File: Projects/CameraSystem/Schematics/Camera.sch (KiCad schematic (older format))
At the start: 10 parts, among them J10 Conn_02x02_Odd_Even, J9 Conn_02x02_Odd_Even, Q2 BC846B_215, U6 OV7670, U7 SIT2001BI-S2-33E-24.000000G

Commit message: feat: symbol assignment updated
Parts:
- C21, C22: footprint Capacitor_SMD:C_0603_1608Metric_Pad1.05x0.95mm_HandSolder -> digikey-footprints:0603
- R26, R27, R28: footprint Resistor_SMD:R_0603_1608Metric_Pad1.05x0.95mm_HandSolder -> digikey-footprints:0603
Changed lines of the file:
@@
 F 0 "C21" H 4825 2300 50  0000 L CNN
 F 1 "100n" H 4825 2100 50  0000 L CNN
-F 2 "Capacitor_SMD:C_0603_1608Metric_Pad1.05x0.95mm_HandSolder" H 4838 2050 50  0001 C CNN
+F 2 "digikey-footprints:0603" H 4838 2050 50  0001 C CNN
 F 3 "" H 4800 2200 50  0001 C CNN
 	1    4800 2200
@@
 F 0 "C22" H 6525 4450 50  0000 L CNN
 F 1 "100n" H 6525 4250 50  0000 L CNN
-F 2 "Capacitor_SMD:C_0603_1608Metric_Pad1.05x0.95mm_HandSolder" H 6538 4200 50  0001 C CNN
+F 2 "digikey-footprints:0603" H 6538 4200 50  0001 C CNN
 F 3 "" H 6500 4350 50  0001 C CNN
 	1    6500 4350
@@
 F 0 "R26" V 8330 4700 50  0000 C CNN
 F 1 "10k" V 8250 4700 50  0000 C CNN
-F 2 "Resistor_SMD:R_0603_1608Metric_Pad1.05x0.95mm_HandSolder" V 8180 4700 50  0001 C CNN
+F 2 "digikey-footprints:0603" V 8180 4700 50  0001 C CNN
 F 3 "" H 8250 4700 50  0001 C CNN
 	1    8250 4700
@@
 F 0 "R27" V 8830 5500 50  0000 C CNN
 F 1 "10k" V 8750 5500 50  0000 C CNN
-F 2 "Resistor_SMD:R_0603_1608Metric_Pad1.05x0.95mm_HandSolder" V 8680 5500 50  0001 C CNN
+F 2 "digikey-footprints:0603" V 8680 5500 50  0001 C CNN
 F 3 "" H 8750 5500 50  0001 C CNN
 	1    8750 5500
@@
 F 0 "R28" V 9130 5250 50  0000 C CNN
 F 1 "4k7" V 9050 5250 50  0000 C CNN
-F 2 "Resistor_SMD:R_0603_1608Metric_Pad1.05x0.95mm_HandSolder" V 8980 5250 50  0001 C CNN
+F 2 "digikey-footprints:0603" V 8980 5250 50  0001 C CNN
 F 3 "" H 9050 5250 50  0001 C CNN
 	1    9050 5250

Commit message: feat: assign footprints
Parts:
- J10, J9: footprint (none) -> Pin_Headers:Pin_Header_Straight_2x02_Pitch2.54mm_SMD
- U6: footprint (none) -> Pin_Headers:Pin_Header_Straight_2x16_Pitch2.54mm
- U7: footprint (none) -> custom-footprints:SiT2001B_SOT23
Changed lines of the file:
@@
 $Descr A4 11693 8268
 encoding utf-8
-Sheet 6 9
+Sheet 5 9
 Title ""
 Date ""
@@
 F 0 "U6" H 5350 2550 60  0000 C CNN
 F 1 "OV7670" H 5350 3550 60  0000 C CNN
-F 2 "" H 5350 3050 60  0001 C CNN
+F 2 "Pin_Headers:Pin_Header_Straight_2x16_Pitch2.54mm" H 5350 3050 60  0001 C CNN
 F 3 "" H 5350 3050 60  0001 C CNN
 	1    5350 3050
@@
 F 0 "U7" H 7700 3700 60  0000 C CNN
 F 1 "SIT2001BI-S2-33E-24.000000G" H 7700 4550 60  0000 C CNN
-F 2 "" H 7700 4050 60  0001 C CNN
+F 2 "custom-footprints:SiT2001B_SOT23" H 7700 4050 60  0001 C CNN
 F 3 "" H 7700 4050 60  0001 C CNN
 	1    7700 4050
@@
 F 0 "J9" H 2700 1717 50  0000 C CNN
 F 1 "Conn_02x02_Odd_Even" H 2700 1626 50  0000 C CNN
-F 2 "" H 2650 1500 50  0001 C CNN
+F 2 "Pin_Headers:Pin_Header_Straight_2x02_Pitch2.54mm_SMD" H 2650 1500 50  0001 C CNN
 F 3 "~" H 2650 1500 50  0001 C CNN
 	1    2650 1500
@@
 F 0 "J10" H 7750 3167 50  0000 C CNN
 F 1 "Conn_02x02_Odd_Even" H 7750 3076 50  0000 C CNN
-F 2 "" H 7700 2950 50  0001 C CNN
+F 2 "Pin_Headers:Pin_Header_Straight_2x02_Pitch2.54mm_SMD" H 7700 2950 50  0001 C CNN
 F 3 "~" H 7700 2950 50  0001 C CNN
 	1    7700 2950

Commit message: feat: start layout
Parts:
- U6: footprint Pin_Headers:Pin_Header_Straight_2x16_Pitch2.54mm -> Pin_Headers:Pin_Header_Straight_2x08_Pitch2.54mm
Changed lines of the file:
@@
 F 0 "U6" H 5350 2550 60  0000 C CNN
 F 1 "OV7670" H 5350 3550 60  0000 C CNN
-F 2 "Pin_Headers:Pin_Header_Straight_2x16_Pitch2.54mm" H 5350 3050 60  0001 C CNN
+F 2 "Pin_Headers:Pin_Header_Straight_2x08_Pitch2.54mm" H 5350 3050 60  0001 C CNN
 F 3 "" H 5350 3050 60  0001 C CNN
 	1    5350 3050

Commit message: linux adaptation
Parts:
- U6: symbol cl-integrated_circuits:OV7670 -> CameraSystem-rescue:OV7670-cl-integrated_circuits
- U7: symbol cl-integrated_circuits:SIT2001BI-S2-33E-24.000000G -> CameraSystem-rescue:SIT2001BI-S2-33E-24.000000G-cl-integrated_circuits
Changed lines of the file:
@@
 $EndDescr
 $Comp
-L cl-integrated_circuits:OV7670 U6
+L CameraSystem-rescue:OV7670-cl-integrated_circuits U6
 U 1 1 5BBB684E
 P 5350 3050
+AR Path="/5BBB684E" Ref="U6"  Part="1"
+AR Path="/5BB4DA63/5BBB684E" Ref="U6"  Part="1"
 F 0 "U6" H 5350 2550 60  0000 C CNN
 F 1 "OV7670" H 5350 3550 60  0000 C CNN
@@
 CAM_CLK
 $Comp
-L cl-integrated_circuits:SIT2001BI-S2-33E-24.000000G U7
+L CameraSystem-rescue:SIT2001BI-S2-33E-24.000000G-cl-integrated_circuits U7
 U 1 1 5BBBA2DE
 P 7700 4050
+AR Path="/5BBBA2DE" Ref="U7"  Part="1"
+AR Path="/5BB4DA63/5BBBA2DE" Ref="U7"  Part="1"
 F 0 "U7" H 7700 3700 60  0000 C CNN
 F 1 "SIT2001BI-S2-33E-24.000000G" H 7700 4550 60  0000 C CNN

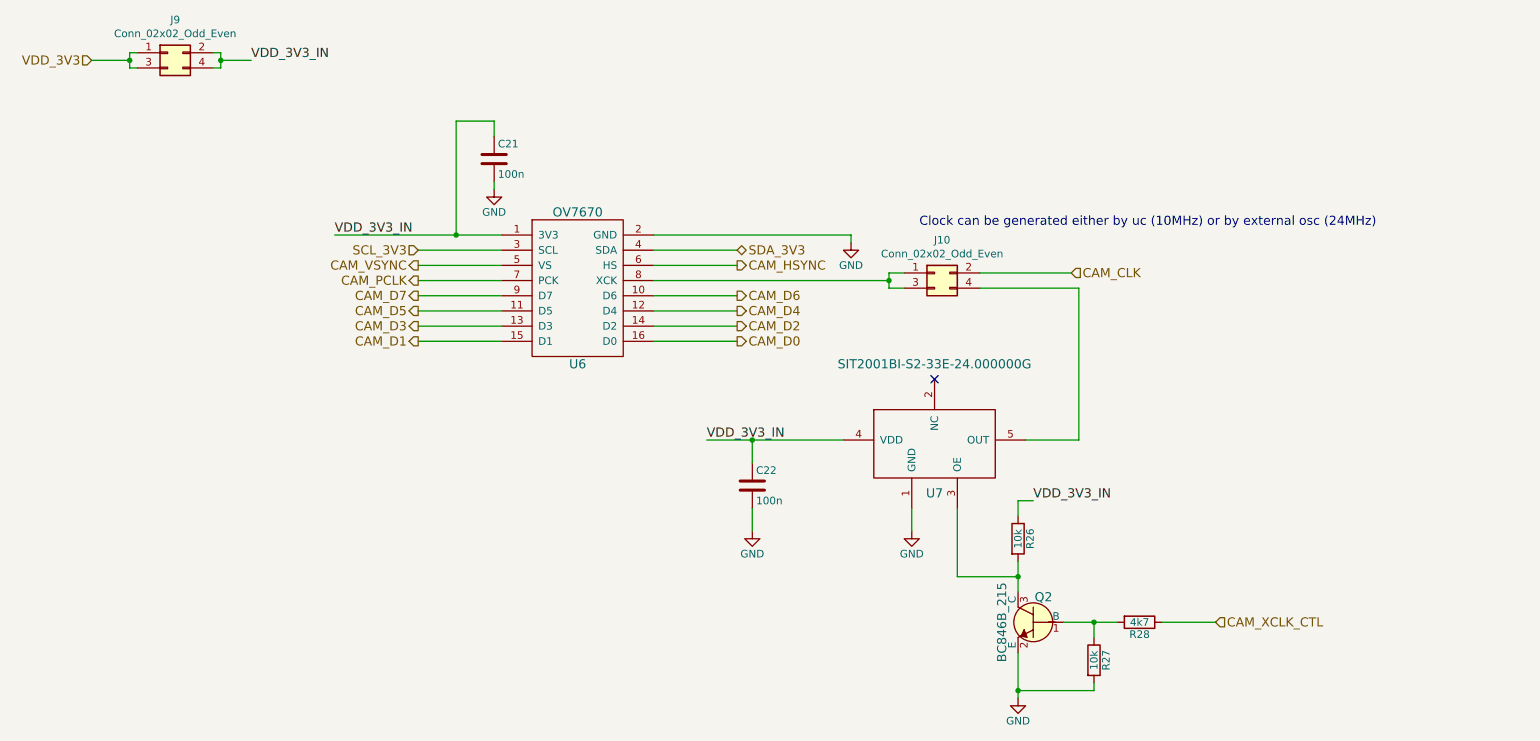
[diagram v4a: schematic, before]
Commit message: camera was updated
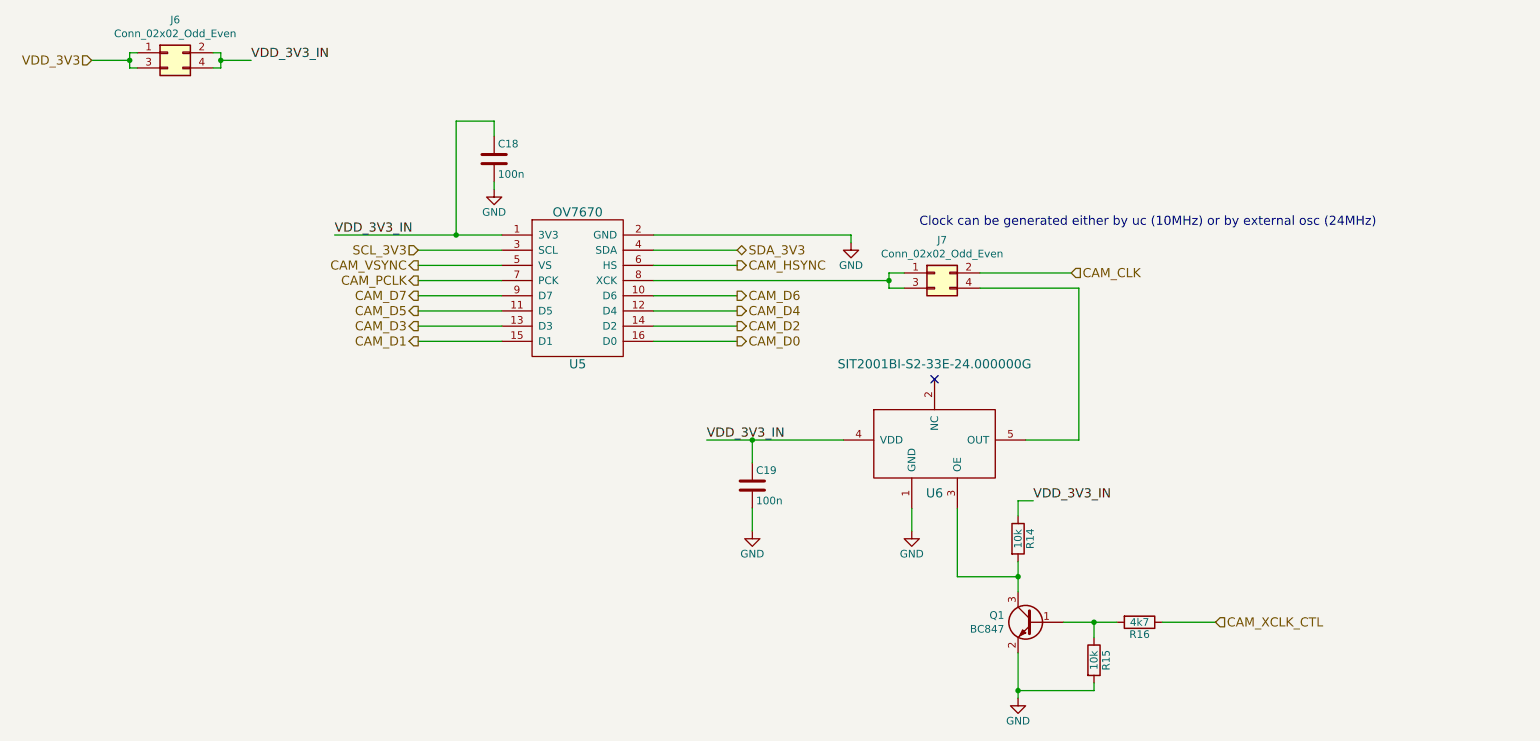
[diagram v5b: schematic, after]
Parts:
- removed Q2: BC846B_215, digikey-footprints:SOT-23-3, symbol CameraSystem-rescue:BC846B_215
- added Q1: BC847, Package_TO_SOT_SMD:SOT-23, symbol Transistor_BJT:BC847
- C18: renamed from C21; footprint digikey-footprints:0603 -> Capacitor_SMD:C_0603_1608Metric_Pad1.05x0.95mm_HandSolder
- C19: renamed from C22; footprint digikey-footprints:0603 -> Capacitor_SMD:C_0603_1608Metric_Pad1.05x0.95mm_HandSolder
- J6: renamed from J9; footprint Pin_Headers:Pin_Header_Straight_2x02_Pitch2.54mm_SMD -> Connector_PinSocket_2.54mm:PinSocket_2x02_P2.54mm_Vertical
- J7: renamed from J10; footprint Pin_Headers:Pin_Header_Straight_2x02_Pitch2.54mm_SMD -> Connector_PinSocket_2.54mm:PinSocket_2x02_P2.54mm_Vertical
- R14: renamed from R26; footprint digikey-footprints:0603 -> Resistor_SMD:R_0603_1608Metric_Pad1.05x0.95mm_HandSolder
- R15: renamed from R27; footprint digikey-footprints:0603 -> Resistor_SMD:R_0603_1608Metric_Pad1.05x0.95mm_HandSolder
- R16: renamed from R28; footprint digikey-footprints:0603 -> Resistor_SMD:R_0603_1608Metric_Pad1.05x0.95mm_HandSolder
- U5: renamed from U6; footprint Pin_Headers:Pin_Header_Straight_2x08_Pitch2.54mm -> Connector_PinSocket_2.54mm:PinSocket_2x08_P2.54mm_Vertical
- renumbered U7 to U6
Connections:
- net GND: now also Q1.2 (E)
- net at R14.2, U6.3 (OE): now also Q1.3 (C)
- net at R15.1, R16.2: now also Q1.1 (B)
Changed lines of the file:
@@
 EESchema Schematic File Version 4
 LIBS:CameraSystem-cache
-EELAYER 26 0
+EELAYER 29 0
 EELAYER END
 $Descr A4 11693 8268
@@
 $EndDescr
 $Comp
-L CameraSystem-rescue:OV7670-cl-integrated_circuits U6
+L CameraSystem-rescue:OV7670-cl-integrated_circuits U?
 U 1 1 5BBB684E
 P 5350 3050
-AR Path="/5BBB684E" Ref="U6"  Part="1"
-AR Path="/5BB4DA63/5BBB684E" Ref="U6"  Part="1"
-F 0 "U6" H 5350 2550 60  0000 C CNN
+AR Path="/5BBB684E" Ref="U?"  Part="1"
+AR Path="/5BB4DA63/5BBB684E" Ref="U5"  Part="1"
+F 0 "U5" H 5350 2550 60  0000 C CNN
 F 1 "OV7670" H 5350 3550 60  0000 C CNN
-F 2 "Pin_Headers:Pin_Header_Straight_2x08_Pitch2.54mm" H 5350 3050 60  0001 C CNN
+F 2 "Connector_PinSocket_2.54mm:PinSocket_2x08_P2.54mm_Vertical" H 5350 3050 60  0001 C CNN
 F 3 "" H 5350 3050 60  0001 C CNN
 	1    5350 3050
@@
 VDD_3V3_IN
 $Comp
-L Device:C C21
+L Device:C C18
 U 1 1 5BBB6CC1
 P 4800 2200
-F 0 "C21" H 4825 2300 50  0000 L CNN
+F 0 "C18" H 4825 2300 50  0000 L CNN
 F 1 "100n" H 4825 2100 50  0000 L CNN
-F 2 "digikey-footprints:0603" H 4838 2050 50  0001 C CNN
+F 2 "Capacitor_SMD:C_0603_1608Metric_Pad1.05x0.95mm_HandSolder" H 4838 2050 50  0001 C CNN
 F 3 "" H 4800 2200 50  0001 C CNN
 	1    4800 2200
@@
 $EndComp
 $Comp
-L power:GND #PWR0131
+L power:GND #PWR025
 U 1 1 5BBB6D0A
 P 4800 2400
-F 0 "#PWR0131" H 4800 2150 50  0001 C CNN
+F 0 "#PWR025" H 4800 2150 50  0001 C CNN
 F 1 "GND" H 4800 2250 50  0000 C CNN
 F 2 "" H 4800 2400 50  0001 C CNN
@@
 	7150 2700 7150 2750
 $Comp
-L power:GND #PWR0132
+L power:GND #PWR027
 U 1 1 5BBB6FDB
 P 7150 2750
-F 0 "#PWR0132" H 7150 2500 50  0001 C CNN
+F 0 "#PWR027" H 7150 2500 50  0001 C CNN
 F 1 "GND" H 7150 2600 50  0000 C CNN
 F 2 "" H 7150 2750 50  0001 C CNN
@@
 CAM_CLK
 $Comp
-L CameraSystem-rescue:SIT2001BI-S2-33E-24.000000G-cl-integrated_circuits U7
+L CameraSystem-rescue:SIT2001BI-S2-33E-24.000000G-cl-integrated_circuits U?
 U 1 1 5BBBA2DE
 P 7700 4050
-AR Path="/5BBBA2DE" Ref="U7"  Part="1"
-AR Path="/5BB4DA63/5BBBA2DE" Ref="U7"  Part="1"
-F 0 "U7" H 7700 3700 60  0000 C CNN
+AR Path="/5BBBA2DE" Ref="U?"  Part="1"
+AR Path="/5BB4DA63/5BBBA2DE" Ref="U6"  Part="1"
+F 0 "U6" H 7700 3700 60  0000 C CNN
 F 1 "SIT2001BI-S2-33E-24.000000G" H 7700 4550 60  0000 C CNN
 F 2 "custom-footprints:SiT2001B_SOT23" H 7700 4050 60  0001 C CNN
@@
 $EndComp
 $Comp
-L power:GND #PWR0133
+L power:GND #PWR028
 U 1 1 5BBBA416
 P 7550 4650
-F 0 "#PWR0133" H 7550 4400 50  0001 C CNN
+F 0 "#PWR028" H 7550 4400 50  0001 C CNN
 F 1 "GND" H 7550 4500 50  0000 C CNN
 F 2 "" H 7550 4650 50  0001 C CNN
@@
 VDD_3V3_IN
 $Comp
-L Device:C C22
+L Device:C C19
 U 1 1 5BBBA5A8
 P 6500 4350
-F 0 "C22" H 6525 4450 50  0000 L CNN
+F 0 "C19" H 6525 4450 50  0000 L CNN
 F 1 "100n" H 6525 4250 50  0000 L CNN
-F 2 "digikey-footprints:0603" H 6538 4200 50  0001 C CNN
+F 2 "Capacitor_SMD:C_0603_1608Metric_Pad1.05x0.95mm_HandSolder" H 6538 4200 50  0001 C CNN
 F 3 "" H 6500 4350 50  0001 C CNN
 	1    6500 4350
@@
 Connection ~ 6500 4050
 $Comp
-L power:GND #PWR0134
+L power:GND #PWR026
 U 1 1 5BBBA64E
 P 6500 4650
-F 0 "#PWR0134" H 6500 4400 50  0001 C CNN
+F 0 "#PWR026" H 6500 4400 50  0001 C CNN
 F 1 "GND" H 6500 4500 50  0000 C CNN
 F 2 "" H 6500 4650 50  0001 C CNN
@@
 NoConn ~ 7700 3650
 $Comp
-L Device:R R26
+L Device:R R14
 U 1 1 5BBBA862
 P 8250 4700
-F 0 "R26" V 8330 4700 50  0000 C CNN
+F 0 "R14" V 8330 4700 50  0000 C CNN
 F 1 "10k" V 8250 4700 50  0000 C CNN
-F 2 "digikey-footprints:0603" V 8180 4700 50  0001 C CNN
+F 2 "Resistor_SMD:R_0603_1608Metric_Pad1.05x0.95mm_HandSolder" V 8180 4700 50  0001 C CNN
 F 3 "" H 8250 4700 50  0001 C CNN
 	1    8250 4700
@@
 	8250 4850 8250 4950
 $Comp
-L CameraSystem-rescue:BC846B_215 Q?
-U 1 1 5BBBB096
-P 8350 5250
-AR Path="/5BBBB096" Ref="Q?"  Part="1"
-AR Path="/5BB4DA63/5BBBB096" Ref="Q2"  Part="1"
-F 0 "Q2" H 8224 5416 60  0000 L CNN
-F 1 "BC846B_215" V 8556 5250 60  0000 C CNN
-F 2 "digikey-footprints:SOT-23-3" H 8550 5450 60  0001 L CNN
-F 3 "https://assets.nexperia.com/documents/data-sheet/BC846_SER.pdf" H 8550 5550 60  0001 L CNN
-F 4 "1727-2920-1-ND" H 8550 5650 60  0001 L CNN "Digi-Key_PN"
-F 5 "BC846B,215" H 8550 5750 60  0001 L CNN "MPN"
-F 6 "Discrete Semiconductor Products" H 8550 5850 60  0001 L CNN "Category"
-F 7 "Transistors - Bipolar (BJT) - Single" H 8550 5950 60  0001 L CNN "Family"
-F 8 "https://assets.nexperia.com/documents/data-sheet/BC846_SER.pdf" H 8550 6050 60  0001 L CNN "DK_Datasheet_Link"
-F 9 "/product-detail/en/nexperia-usa-inc/BC846B,215/1727-2920-1-ND/763459" H 8550 6150 60  0001 L CNN "DK_Detail_Page"
-F 10 "TRANS NPN 65V 0.1A SOT23" H 8550 6250 60  0001 L CNN "Description"
-F 11 "Nexperia USA Inc." H 8550 6350 60  0001 L CNN "Manufacturer"
-F 12 "Active" H 8550 6450 60  0001 L CNN "Status"
-	1    8350 5250
-	-1   0    0    -1
-$EndComp
-$Comp
-L Device:R R27
+L Device:R R15
 U 1 1 5BBBB16C
 P 8750 5500
-F 0 "R27" V 8830 5500 50  0000 C CNN
+F 0 "R15" V 8830 5500 50  0000 C CNN
 F 1 "10k" V 8750 5500 50  0000 C CNN
-F 2 "digikey-footprints:0603" V 8680 5500 50  0001 C CNN
+F 2 "Resistor_SMD:R_0603_1608Metric_Pad1.05x0.95mm_HandSolder" V 8680 5500 50  0001 C CNN
 F 3 "" H 8750 5500 50  0001 C CNN
 	1    8750 5500
@@
 $EndComp
 $Comp
-L power:GND #PWR0135
+L power:GND #PWR029
 U 1 1 5BBBB1AD
 P 8250 5750
-F 0 "#PWR0135" H 8250 5500 50  0001 C CNN
+F 0 "#PWR029" H 8250 5500 50  0001 C CNN
 F 1 "GND" H 8250 5600 50  0000 C CNN
 F 2 "" H 8250 5750 50  0001 C CNN
@@
 	8250 5450 8250 5700
 $Comp
-L Device:R R28
+L Device:R R16
 U 1 1 5BBBB238
 P 9050 5250
-F 0 "R28" V 9130 5250 50  0000 C CNN
+F 0 "R16" V 9130 5250 50  0000 C CNN
 F 1 "4k7" V 9050 5250 50  0000 C CNN
-F 2 "digikey-footprints:0603" V 8980 5250 50  0001 C CNN
+F 2 "Resistor_SMD:R_0603_1608Metric_Pad1.05x0.95mm_HandSolder" V 8980 5250 50  0001 C CNN
 F 3 "" H 9050 5250 50  0001 C CNN
 	1    9050 5250
@@
 	8250 4950 8250 5050
 $Comp
-L Connector_Generic:Conn_02x02_Odd_Even J9
+L Connector_Generic:Conn_02x02_Odd_Even J6
 U 1 1 5BC287BF
 P 2650 1500
-F 0 "J9" H 2700 1717 50  0000 C CNN
+F 0 "J6" H 2700 1717 50  0000 C CNN
 F 1 "Conn_02x02_Odd_Even" H 2700 1626 50  0000 C CNN
-F 2 "Pin_Headers:Pin_Header_Straight_2x02_Pitch2.54mm_SMD" H 2650 1500 50  0001 C CNN
+F 2 "Connector_PinSocket_2.54mm:PinSocket_2x02_P2.54mm_Vertical" H 2650 1500 50  0001 C CNN
 F 3 "~" H 2650 1500 50  0001 C CNN
 	1    2650 1500
@@
 $EndComp
 $Comp
-L Connector_Generic:Conn_02x02_Odd_Even J10
+L Connector_Generic:Conn_02x02_Odd_Even J7
 U 1 1 5BC289B3
 P 7700 2950
-F 0 "J10" H 7750 3167 50  0000 C CNN
+F 0 "J7" H 7750 3167 50  0000 C CNN
 F 1 "Conn_02x02_Odd_Even" H 7750 3076 50  0000 C CNN
-F 2 "Pin_Headers:Pin_Header_Straight_2x02_Pitch2.54mm_SMD" H 7700 2950 50  0001 C CNN
+F 2 "Connector_PinSocket_2.54mm:PinSocket_2x02_P2.54mm_Vertical" H 7700 2950 50  0001 C CNN
 F 3 "~" H 7700 2950 50  0001 C CNN
 	1    7700 2950
 	1    0    0    -1
 $EndComp
+$Comp
+L Transistor_BJT:BC847 Q1
+U 1 1 5CAB30D3
+P 8350 5250
+F 0 "Q1" H 8541 5296 50  0000 L CNN
+F 1 "BC847" H 8541 5205 50  0000 L CNN
+F 2 "Package_TO_SOT_SMD:SOT-23" H 8550 5175 50  0001 L CIN
+F 3 "http://www.infineon.com/dgdl/Infineon-BC847SERIES_BC848SERIES_BC849SERIES_BC850SERIES-DS-v01_01-en.pdf?fileId=db3a304314dca389011541d4630a1657" H 8350 5250 50  0001 L CNN
+	1    8350 5250
+	-1   0    0    -1
+$EndComp
 $EndSCHEMATC

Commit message: camera layout updated
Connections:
- net CAM_CLK: now also J7.4 (Pin_4); no longer J7.2 (Pin_2)
- net at U6.5 (OUT): now also J7.2 (Pin_2); no longer J7.4 (Pin_4)
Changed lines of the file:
@@
 	7400 3050 7500 3050
 Connection ~ 7400 3000
-Wire Wire Line
-	8000 2950 8600 2950
-Text HLabel 8600 2950 2    60   Input ~ 0
+Text HLabel 8150 3050 2    60   Input ~ 0
 CAM_CLK
 $Comp
@@
 CAM_XCLK_CTL
 Wire Wire Line
-	8000 3050 8650 3050
-Wire Wire Line
-	8650 3050 8650 4050
-Wire Wire Line
 	8650 4050 8300 4050
 Text Notes 7600 2650 0    60   ~ 0
@@
 	-1   0    0    -1
 $EndComp
+Wire Wire Line
+	8000 3050 8150 3050
+Wire Wire Line
+	8000 2950 8650 2950
+Wire Wire Line
+	8650 2950 8650 4050
 $EndSCHEMATC
